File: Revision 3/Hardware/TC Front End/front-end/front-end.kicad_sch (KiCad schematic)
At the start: 0 parts

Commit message: Project template fully initialized
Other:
- sheet Project Architecture renamed Section B - Title B
- removed sheet Block Diagram
- removed sheet Power - Sequencing
- sheet Section B - Title B: file Project Architecture.kicad_sch -> Section B - TItle B.kicad_sch
- note added: "Interface"
- note removed: "Block Diagram"
- note removed: "Power - Sequencing"
- note removed: "Project Architecture"
- note removed: "Random Sheet 1"
- note removed: "Random Sheet 2"
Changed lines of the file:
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@@
 		)
 	)
-	(text "Random Sheet 1"
+	(text "..........................................."
 		(exclude_from_sim no)
 		(at 45.72 106.68 0)
@@
 		)
 	)
-	(text "Random Sheet 2"
+	(text "..........................................."
 		(exclude_from_sim no)
 		(at 45.72 114.3 0)
@@
 		)
 	)
-	(text "Power - Sequencing"
+	(text "..........................................."
 		(exclude_from_sim no)
 		(at 45.72 121.92 0)
@@
 		)
 	)
-	(text "Block Diagram"
+	(text "Interface"
 		(exclude_from_sim no)
 		(at 45.72 91.44 0)
@@
 		)
 	)
-	(text "Project Architecture"
+	(text "Revision History"
 		(exclude_from_sim no)
 		(at 45.72 99.06 0)
@@
 		)
 	)
-	(text "Revision History"
+	(text "..........................................."
 		(exclude_from_sim no)
 		(at 45.72 129.54 0)
@@
 			(type dot)
 			(color 0 0 0 1)
-		)
-	)
-	(sheet
-		(at 340.36 313.69)
-		(size 35.56 5.08)
-		(exclude_from_sim no)
-		(in_bom yes)
-		(on_board yes)
-		(dnp no)
-		(stroke
-			(width 0.1524)
-			(type solid)
-		)
-		(fill
-			(color 0 0 0 0.0000)
-		)
-		(property "Sheetname" "Power - Sequencing"
-			(at 340.36 312.6609 0)
-			(effects
-				(font
-					(face "Times New Roman")
-					(size 1.905 1.905)
-					(bold yes)
-					(color 0 0 0 1)
-				)
-				(justify left bottom)
-			)
-		)
-		(property "Sheetfile" "Power - Sequencing.kicad_sch"
-			(at 341.63 314.96 0)
-			(effects
-				(font
-					(face "Arial")
-					(size 1.27 1.27)
-				)
-				(justify left top)
-			)
-		)
-		(instances
-			(project "front-end"
-				(path "/0650c7a8-acba-429c-9f8e-eec0baf0bc1c"
-					(page "6")
-				)
-			)
-		)
-	)
-	(sheet
-		(at 299.72 302.26)
-		(size 35.56 5.08)
-		(exclude_from_sim no)
-		(in_bom yes)
-		(on_board yes)
-		(dnp no)
-		(stroke
-			(width 0.1524)
-			(type solid)
-		)
-		(fill
-			(color 0 0 0 0.0000)
-		)
-		(property "Sheetname" "Block Diagram"
-			(at 299.72 301.2309 0)
-			(effects
-				(font
-					(face "Times New Roman")
-					(size 1.905 1.905)
-					(bold yes)
-					(color 0 0 0 1)
-				)
-				(justify left bottom)
-			)
-		)
-		(property "Sheetfile" "Block Diagram.kicad_sch"
-			(at 300.99 303.53 0)
-			(effects
-				(font
-					(face "Arial")
-					(size 1.27 1.27)
-				)
-				(justify left top)
-			)
-		)
-		(instances
-			(project "front-end"
-				(path "/0650c7a8-acba-429c-9f8e-eec0baf0bc1c"
-					(page "2")
-				)
-			)
 		)
 	)
@@
 			(project "front-end"
 				(path "/0650c7a8-acba-429c-9f8e-eec0baf0bc1c"
-					(page "7")
+					(page "3")
 				)
 			)
@@
 	)
 	(sheet
-		(at 299.72 313.69)
+		(at 299.72 302.26)
 		(size 35.56 5.08)
 		(exclude_from_sim no)
@@
 			(color 0 0 0 0.0000)
 		)
-		(property "Sheetname" "Project Architecture"
-			(at 299.72 312.6609 0)
+		(property "Sheetname" "Section B - Title B"
+			(at 299.72 301.2309 0)
 			(effects
 				(font
@@
 			)
 		)
-		(property "Sheetfile" "Project Architecture.kicad_sch"
-			(at 300.99 314.96 0)
+		(property "Sheetfile" "Section B - TItle B.kicad_sch"
+			(at 300.99 303.53 0)
 			(effects
 				(font
@@
 			(project "front-end"
 				(path "/0650c7a8-acba-429c-9f8e-eec0baf0bc1c"
-					(page "3")
+					(page "Interface")
 				)
 			)

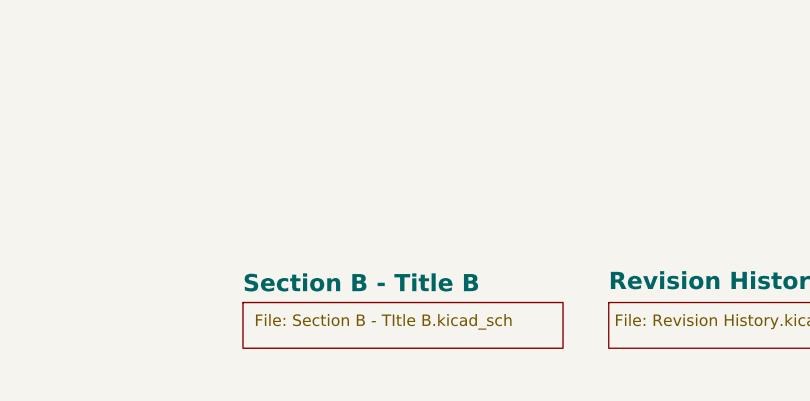
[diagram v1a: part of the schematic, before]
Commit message: fix typo in page numbers
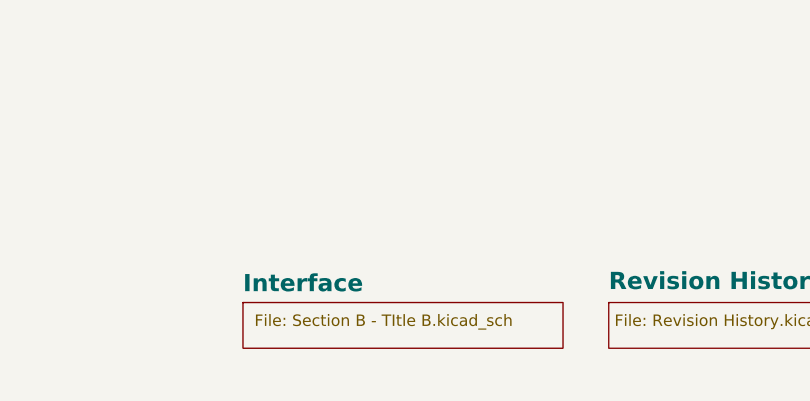
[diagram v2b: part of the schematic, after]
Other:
- sheet Section B - Title B renamed Interface
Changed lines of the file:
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@@
 			(color 0 0 0 0.0000)
 		)
-		(property "Sheetname" "Section B - Title B"
+		(property "Sheetname" "Interface"
 			(at 299.72 301.2309 0)
 			(effects
@@
 			(project "front-end"
 				(path "/0650c7a8-acba-429c-9f8e-eec0baf0bc1c"
-					(page "Interface")
+					(page "2")
 				)
 			)
